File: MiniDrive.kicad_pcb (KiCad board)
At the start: 2 copper layers, 25 x 40.1 mm, 24 parts, among them J1 Conn_LED, J2 Conn_24V, J3 Dimmer, U1 TPS92200

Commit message: Clean up schematic and layout
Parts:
- removed TP4: TestPoint, TestPoint:TestPoint_THTPad_D1.5mm_Drill0.7mm
- removed TP5: Current Meter, TestPoint:TestPoint_2Pads_Pitch2.54mm_Drill0.8mm
- added F1: Polyfuse, Fuse:Fuse_1206_3216Metric, F.Cu at (132.5, 93.5)
- added TP3: Current Meter, TestPoint:TestPoint_2Pads_Pitch2.54mm_Drill0.8mm, F.Cu at (149.2, 87.8)
- C1, C3: footprint Capacitor_SMD:C_1210_3225Metric_Pad1.33x2.70mm_HandSolder -> Capacitor_SMD:C_1210_3225Metric
- C2, C4: footprint Capacitor_SMD:C_1206_3216Metric_Pad1.33x1.80mm_HandSolder -> Capacitor_SMD:C_1206_3216Metric
- C5: footprint Capacitor_SMD:C_0402_1005Metric_Pad0.74x0.62mm_HandSolder -> Capacitor_SMD:C_0402_1005Metric
- R1, R2, R3, R4, R5: footprint Resistor_SMD:R_1206_3216Metric_Pad1.30x1.75mm_HandSolder -> Resistor_SMD:R_0805_2012Metric
- U1: footprint Package_TO_SOT_SMD:SOT-23-6_Handsoldering -> Package_TO_SOT_SMD:SOT-23-6
- moved D1 3.38 mm to (133.8, 114.3)
- moved R6 3.14 mm to (133.5, 117.6)
- moved J2 3.00 mm to (141.5, 112.7)
- moved TP2 2.10 mm to (149.5, 104.5)
- moved R1 1.95 mm to (132.5, 97.5)
- moved R3 1.32 mm to (142.8, 109.2), turned to 180 degrees
- moved R4 1.23 mm to (145.5, 108.5)
- moved R2 0.98 mm to (135.5, 97.5)
- moved C5 0.72 mm to (134.0, 100.0)
- moved TP1 0.52 mm to (147.0, 104.5)
- moved C2 0.50 mm to (137.0, 107.0)
- moved C3 0.25 mm to (137.0, 104.2)
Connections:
- R1 pad 2: Net-(J1-Pin_1) -> Net-(F1-Pad1)
- R2 pad 1: Net-(J1-Pin_1) -> Net-(F1-Pad1)
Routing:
- net Net-(U1-SW): track 9.70 -> 0.55 mm
- net +24V: track 23.3 -> 19.7 mm
- net Net-(J3-Pin_2): track 30.7 -> 33.3 mm
- net GND: track 36.0 -> 33.8 mm
- net Net-(U1-FB): track 3.66 -> 3.12 mm
- added copper zone on F.Cu, net Net-(F1-Pad1)
- added copper zone on F.Cu, net Net-(U1-SW)
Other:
- board text added: "MiniDrive LED Driver Revision 1"
- board text removed: "MiniDrive LED Driver Revision 0"

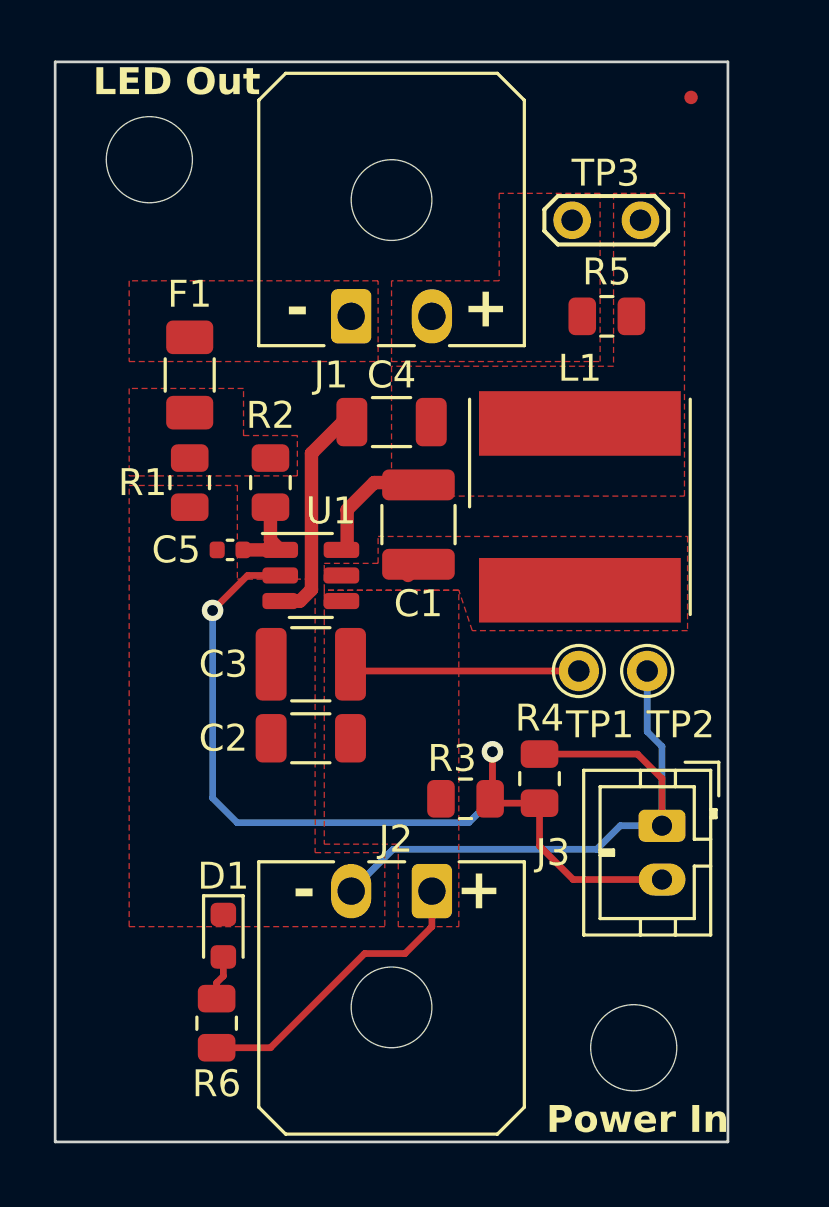
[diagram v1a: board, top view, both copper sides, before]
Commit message: Revert back to 1206 resistors
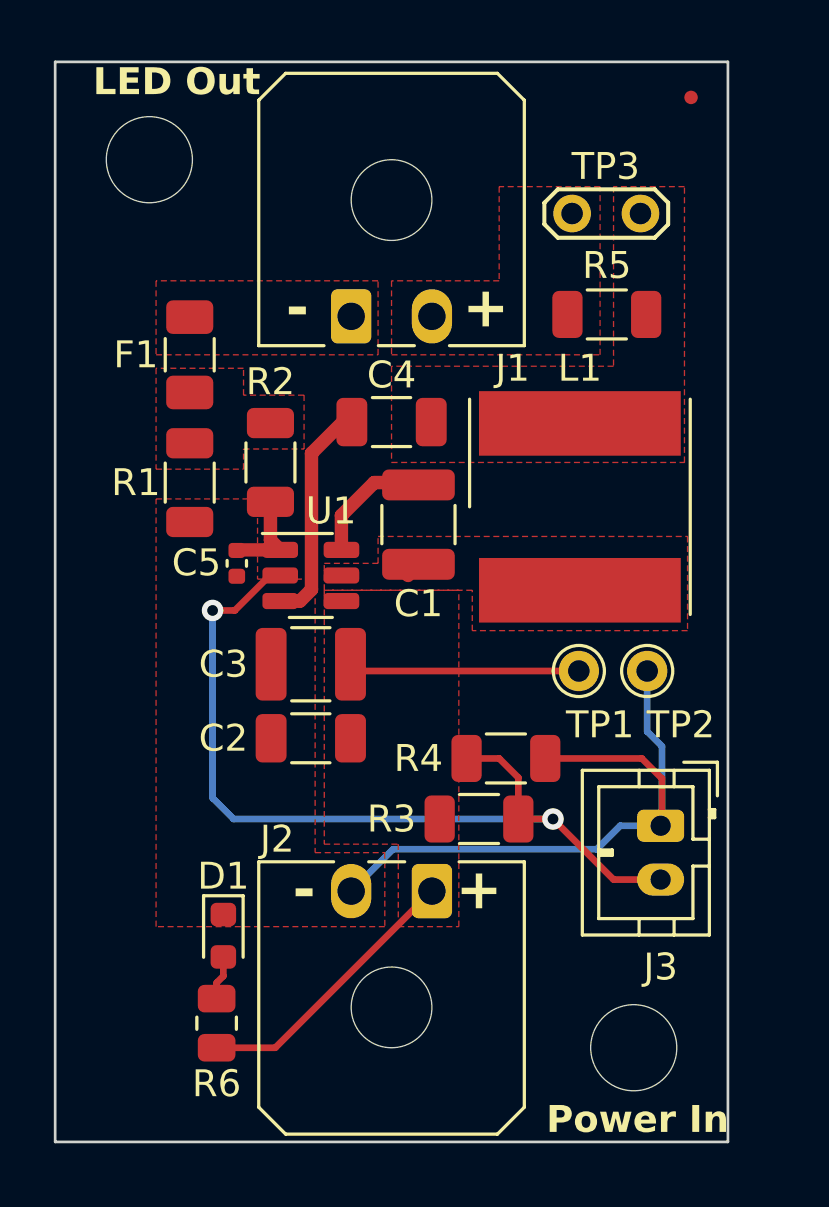
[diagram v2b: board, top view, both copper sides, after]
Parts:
- R1, R2, R3, R4, R5: footprint Resistor_SMD:R_0805_2012Metric -> Resistor_SMD:R_1206_3216Metric
- moved R4 1.46 mm to (144.2, 107.8), turned to 180 degrees
- moved R3 0.90 mm to (143.2, 110.0)
- moved F1 0.75 mm to (132.5, 92.8)
- moved R2 0.75 mm to (135.5, 96.8)
- moved C5 0.56 mm to (134.2, 100.5), turned to -90 degrees
- moved TP3 0.25 mm to (149.2, 87.5)
- moved R5 0.07 mm to (148.0, 91.2)
- moved J3 0.05 mm to (150.0, 110.2)
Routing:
- net +24V: track 19.7 -> 18.9 mm

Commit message: Minor tweaks, remove F1
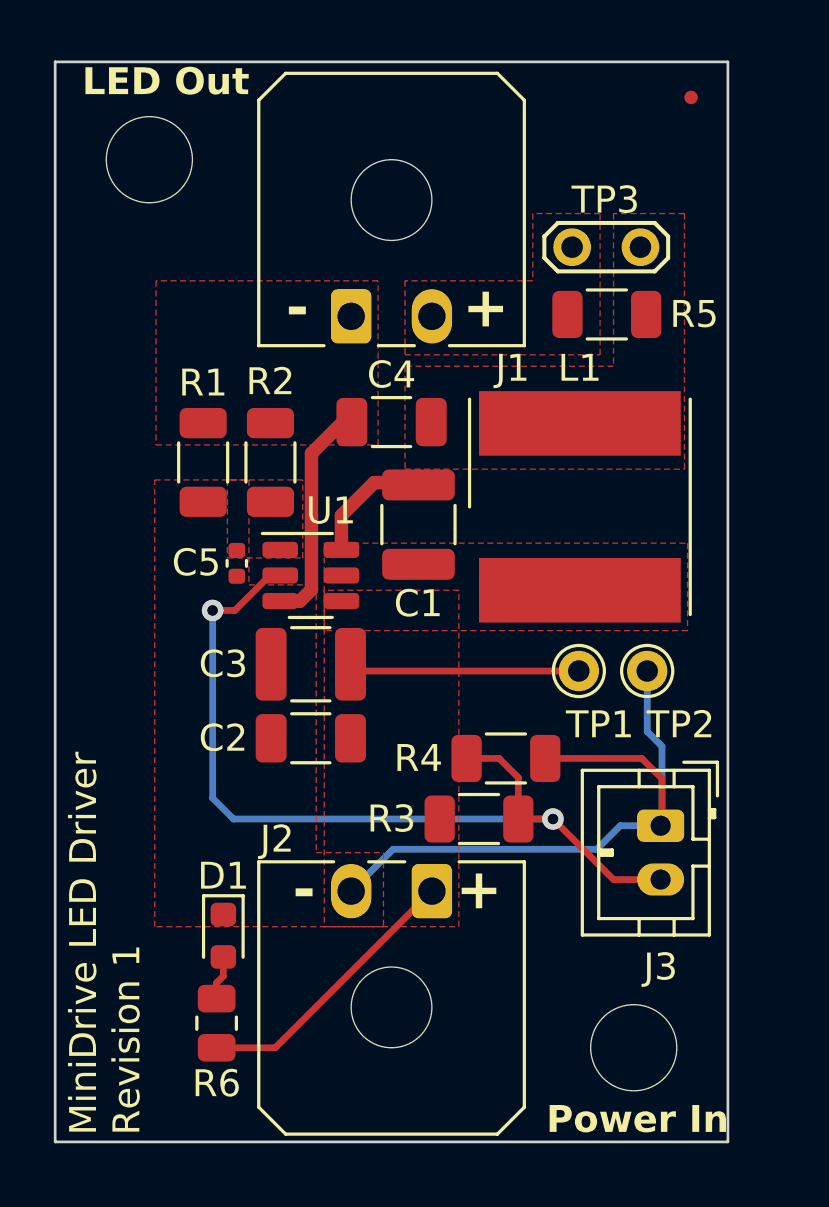
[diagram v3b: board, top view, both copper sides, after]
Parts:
- removed F1: Polyfuse, Fuse:Fuse_1206_3216Metric
- moved TP3 1.25 mm to (149.2, 88.8)
- moved R1 0.90 mm to (133.0, 96.8)
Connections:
- R1 pad 2: Net-(F1-Pad1) -> Net-(J1-Pin_1)
- R2 pad 1: Net-(F1-Pad1) -> Net-(J1-Pin_1)
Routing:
- net Net-(U1-FB): track 3.37 -> 0.00 mm
- net Net-(U1-SW): track 0.55 -> 0.00 mm
- added copper zone on F.Cu, net Net-(U1-FB)
- removed copper zone on F.Cu, net Net-(F1-Pad1)
